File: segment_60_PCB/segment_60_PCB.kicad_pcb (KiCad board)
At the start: 2 copper layers, 119 parts, among them J1 MDB-9M, J2 #AVR-ISP-6, SW1 SW_Push_45deg, SW10 SW_Push_45deg, SW11 SW_Push_45deg, SW12 SW_Push_45deg, SW13 SW_Push_45deg, SW14 SW_Push_45deg, SW15 SW_Push_45deg, SW16 SW_Push_45deg, SW17 SW_Push_45deg, SW18 SW_Push_45deg, SW19 SW_Push_45deg, SW2 SW_Push_45deg, SW20 SW_Push_45deg, SW21 SW_Push_45deg, SW22 SW_Push_45deg, SW23 SW_Push_45deg, SW24 SW_Push_45deg, SW25 SW_Push_45deg, SW26 SW_Push_45deg, SW27 SW_Push_45deg, SW28 SW_Push_45deg, SW29 SW_Push_45deg, SW3 SW_Push_45deg, SW30 SW_Push_45deg, SW31 SW_Push_45deg, SW32 SW_Push_45deg, SW33 SW_Push_45deg, SW34 SW_Push_45deg, SW35 SW_Push_45deg, SW36 SW_Push_45deg, SW37 SW_Push_45deg, SW38 SW_Push_45deg, SW39 SW_Push_45deg, SW4 SW_Push_45deg, SW40 SW_Push_45deg, SW41 SW_Push_45deg, SW42 SW_Push_45deg, SW43 SW_Push_45deg, SW44 SW_Push_45deg, SW45 SW_Push_45deg, SW46 SW_Push_45deg, SW47 SW_Push_45deg, SW48 SW_Push_45deg, SW49 SW_Push_45deg, SW5 SW_Push_45deg, SW50 SW_Push_45deg, SW51 SW_Push_45deg, SW52 SW_Push_45deg, SW53 SW_Push_45deg, SW54 SW_Push_45deg, SW55 SW_Push_45deg, SW56 SW_Push_45deg, SW57 SW_Push_45deg, SW58 SW_Push_45deg, SW59 SW_Push_45deg, SW6 SW_Push_45deg, SW60 SW_Push_45deg, SW61 SW_Push_45deg, SW62 SW_Push_45deg, SW63 SW_Push_45deg, SW64 SW_Push_45deg, SW65 SW_Push_45deg, SW7 SW_Push_45deg, SW8 SW_Push_45deg, SW9 SW_Push_45deg, U1 ATmega328P-PU, U10 74HC365, U11 74HC365, U12 74HC365, U13 74HC365, U14 74HC365, U15 74HC365, U16 74HC365, U17 74HC365, U2 74HC138, U3 74HC138, U4 74HC365, U5 74HC365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

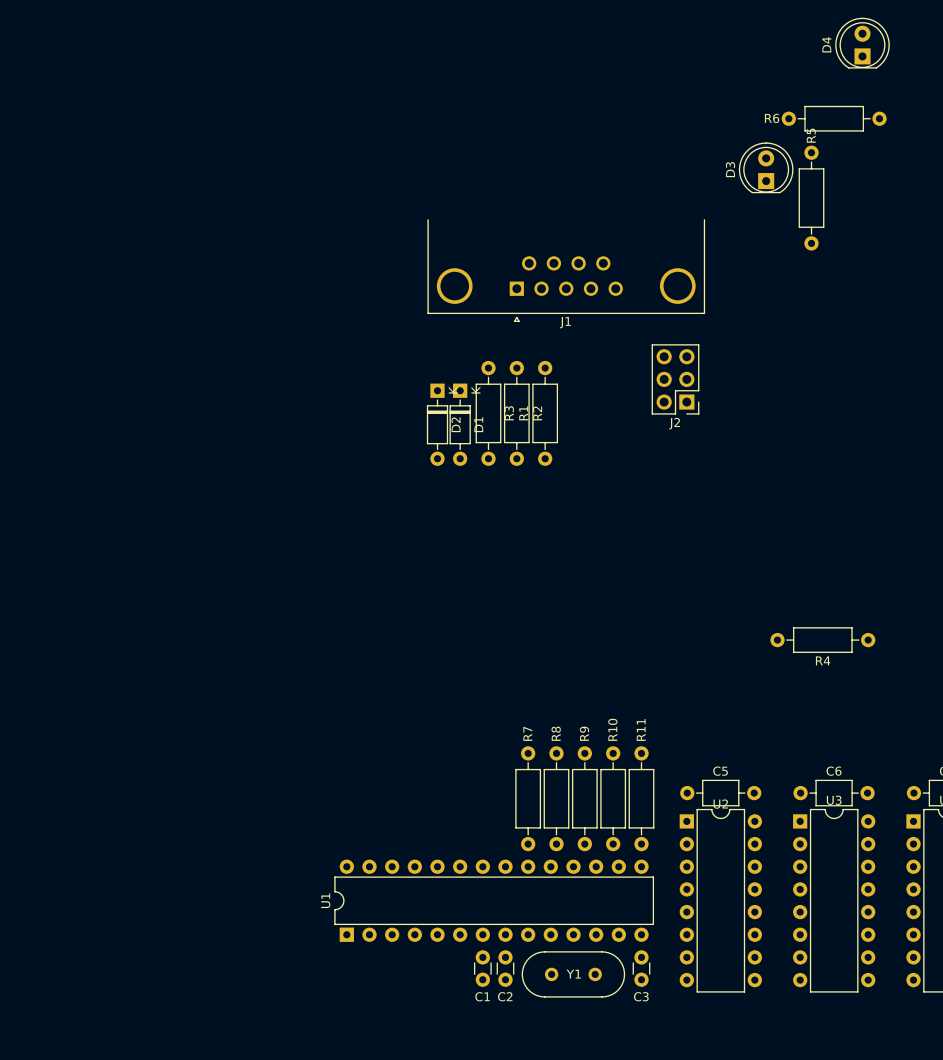
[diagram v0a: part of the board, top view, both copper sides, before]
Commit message: Continued organizing footprints and minor layout changes to control hardware.
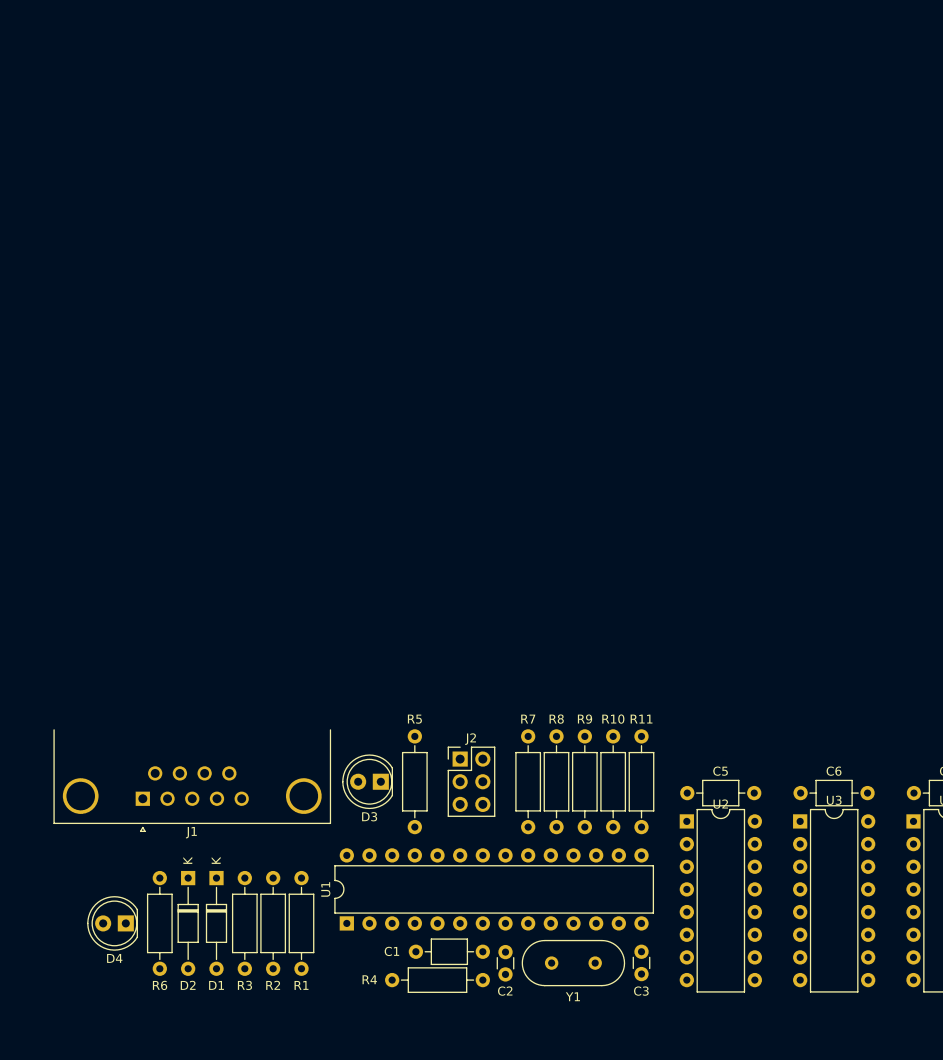
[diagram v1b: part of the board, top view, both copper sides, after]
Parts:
- C1: footprint Capacitor_THT:C_Disc_D3.0mm_W1.6mm_P2.50mm -> Capacitor_THT:C_Axial_L3.8mm_D2.6mm_P7.50mm_Horizontal
- D1, D2: footprint Diode_THT:D_DO-35_SOD27_P7.62mm_Horizontal -> Diode_THT:D_DO-35_SOD27_P10.16mm_Horizontal
- moved D4 127.5 mm to (93.3, 110.5), turned to 180 degrees
- moved R6 110.5 mm to (97.2, 105.4), turned to 270 degrees
- moved D3 80.0 mm to (121.9, 94.6), turned to 180 degrees
- moved R5 79.1 mm to (125.7, 89.5)
- moved J1 70.9 mm to (95.2, 96.5)
- moved R3 63.3 mm to (106.7, 105.4)
- moved R1 63.3 mm to (113.0, 115.6)
- moved R2 63.3 mm to (109.9, 105.4)
- moved D2 61.3 mm to (100.3, 105.4)
- moved D1 61.1 mm to (103.5, 105.4)
- moved R4 57.6 mm to (133.3, 116.8)
- moved J2 47.4 mm to (130.8, 92.1), turned to 0 degrees
- moved R10 1.91 mm to (148.0, 89.5)
- moved R11 1.91 mm to (151.1, 89.5)
- moved R7 1.91 mm to (138.4, 89.5)
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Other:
- net class Default: clearance 0.2 -> 0.4572; trace_width 0.25 -> 0.4572
- rule trace_clearance: 0.2 -> 0.4572

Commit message: Added remaining footprints, changed library paths to be relative.
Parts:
- added C4: 4.7u, Capacitor_THT:CP_Axial_L11.0mm_D5.0mm_P18.00mm_Horizontal, F.Cu at (103.5, 101.6)
- added F1: 100mA, Fuse:Fuse_Littelfuse_395Series, F.Cu at (113.0, 101.6)
- added SW66: SW_Push, Button_Switch_THT:SW_PUSH_6mm, F.Cu at (126.7, 97.8)
- added SW67: SW_Push, Button_Switch_THT:SW_PUSH_6mm, F.Cu at (118.1, 97.8)
- C1: footprint Capacitor_THT:C_Axial_L3.8mm_D2.6mm_P7.50mm_Horizontal -> Capacitor_THT:C_Axial_L3.8mm_D2.6mm_P10.00mm_Horizontal
- moved R5 28.3 mm to (133.3, 116.8), turned to 180 degrees
- moved J2 24.0 mm to (111.8, 106.7), turned to 270 degrees
- moved D3 22.5 mm to (116.8, 116.5), turned to 90 degrees
- moved R4 17.3 mm to (135.3, 99.7), turned to 90 degrees
- moved D4 16.4 mm to (108.6, 116.5), turned to 90 degrees
- moved R2 15.3 mm to (94.6, 106.0)
- moved R3 15.3 mm to (91.4, 106.0)
- moved D1 15.3 mm to (88.3, 106.0)
- moved D2 15.3 mm to (85.1, 106.0)
- moved R1 15.3 mm to (97.8, 116.2)
- moved R6 3.86 mm to (101.0, 106.0)
- moved J1 1.80 mm to (94.0, 95.2)
- moved C1 0.08 mm to (133.3, 113.7)
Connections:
- J1 pad 3: Net-(F1-Pad2) -> SCK
- J1 pad 4: SCK -> RST
- J1 pad 5: RST -> BOOT
- J1 pad 9: GND -> Net-(F1-Pad2)
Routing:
- net XTAL2: track 0.00 -> 12.0 mm
- net XTAL1: track 0.00 -> 10.5 mm
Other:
- net class Default: clearance 0.4572 -> 0.3; trace_width 0.4572 -> 0.3
- rule trace_clearance: 0.4572 -> 0.3
- board text added: "ADDR"
- board text added: "BANK A"
- board text added: "BANK B"
- board text added: "BOOT"
- board text added: "RESET"

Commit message: Tweaked layout.
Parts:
- moved F1 8.08 mm to (107.3, 107.3), turned to 0 degrees
- moved D4 6.81 mm to (105.4, 122.6)
- moved J2 6.25 mm to (109.2, 112.4)
- moved D3 6.06 mm to (117.5, 122.6)
- moved U1 5.75 mm to (117.5, 116.2)
- moved R10 5.75 mm to (147.3, 95.2)
- moved R7 5.75 mm to (137.8, 95.2)
- moved D1 5.75 mm to (87.6, 111.8)
- moved D2 5.75 mm to (84.5, 111.8)
- moved J1 5.75 mm to (93.3, 101.0)
- moved R1 5.75 mm to (97.2, 121.9)
- moved R6 5.75 mm to (100.3, 111.8)
- moved C2 5.75 mm to (135.3, 121.9)
- moved C4 5.75 mm to (102.9, 107.3)
- moved R11 5.75 mm to (150.5, 95.2)
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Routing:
- net XTAL2: track 12.0 -> 0.00 mm
- net XTAL1: track 10.5 -> 0.00 mm
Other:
- board text removed: "ADDR"
- board text removed: "BANK A"
- board text removed: "BANK B"

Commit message: Updated layout; changed row pullup resistors to a single resistor network
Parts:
- removed J2: #AVR-ISP-6, Connector_PinHeader_2.54mm:PinHeader_2x03_P2.54mm_Vertical
- removed R10, R11, R7, R8, R9: 10k, Resistor_THT:R_Axial_DIN0207_L6.3mm_D2.5mm_P10.16mm_Horizontal
- added RN1: 10k, Resistor_THT:R_Array_SIP7, F.Cu at (233.7, 102.9)
- J1: value MDB-9M -> BREAKOUT; footprint Connector_Dsub:DSUB-9_Female_Horizontal_P2.77x2.84mm_EdgePinOffset4.94mm_Housed_MountingHolesOffset7.48mm -> Connector_PinHeader_2.54mm:PinHeader_2x06_P2.54mm_Vertical
- moved D3 134.3 mm to (249.6, 98.1)
- moved R3 123.0 mm to (213.4, 122.6), turned to 90 degrees
- moved SW67 120.1 mm to (237.5, 99.1), turned to 180 degrees
- moved R2 116.7 mm to (210.2, 122.6), turned to 90 degrees
- moved D1 116.2 mm to (203.8, 112.4)
- moved D2 116.2 mm to (200.7, 112.4)
- moved R5 110.4 mm to (241.3, 102.9), turned to 0 degrees
- moved R1 110.3 mm to (207.0, 112.4), turned to 270 degrees
- moved J1 107.4 mm to (200.7, 106.0), turned to 90 degrees
- moved R4 102.3 mm to (233.7, 120.7), turned to 180 degrees
- moved C2 101.0 mm to (236.2, 120.0)
- moved C1 101.0 mm to (233.6, 117.5)
- moved U1 101.0 mm to (218.4, 114.3)
- moved Y1 101.0 mm to (241.4, 118.7)
- moved C3 101.0 mm to (251.5, 117.5)
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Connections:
- D1 pad 1: Net-(D1-Pad1) -> USB-
- D2 pad 1: Net-(D2-Pad1) -> USB+
- D3 pad 2: LED0 -> VCC
- J1 pad 2: MOSI -> Net-(F1-Pad2)
- J1 pad 4: RST -> MOSI
- J1 pad 5: BOOT -> RST
- J1 pad 7: Net-(D1-Pad1) -> TXD
- J1 pad 8: Net-(D2-Pad1) -> RXD
- J1 pad 9: Net-(F1-Pad2) -> BOOT
- R1 pad 1: VCC -> USB-
- R1 pad 2: Net-(D2-Pad1) -> VCC
- R2 pad 1: Net-(D2-Pad1) -> D-
- R2 pad 2: D- -> USB-
- R3 pad 1: Net-(D1-Pad1) -> D+
- R3 pad 2: D+ -> USB+
- R5 pad 2: GND -> LED0
- U1 pad 14: ROW0 -> /SEL4
- U1 pad 15: ROW1 -> BOOT
- U1 pad 2: BOOT -> RXD
- U1 pad 23: ROW2 -> ROW0
- U1 pad 24: ROW3 -> ROW1
- U1 pad 25: ROW4 -> ROW2
- U1 pad 26: Net-(U1-Pad26) -> ROW3
- U1 pad 27: Net-(U1-Pad27) -> ROW4
- U1 pad 28: Net-(U1-Pad28) -> ROW5
- U1 pad 3: Net-(U1-Pad3) -> TXD
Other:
- board text removed: "BOOT"
- board text removed: "RESET"

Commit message: added border, changed J1 footprint and model
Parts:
- J1: footprint Connector_PinHeader_2.54mm:PinHeader_2x06_P2.54mm_Vertical -> Connector_IDC:IDC-Header_2x06_P2.54mm_Vertical
- moved F1 15.3 mm to (193.4, 119.4), turned to 90 degrees
- moved SW67 5.08 mm to (237.6, 104.1)
- moved SW66 5.03 mm to (224.9, 104.1)
- moved R5 4.44 mm to (241.3, 107.3)
- moved RN1 4.44 mm to (233.7, 107.3)
- moved D3 4.09 mm to (249.6, 102.2)
- moved C1 3.81 mm to (233.6, 121.3)
- moved C2 3.81 mm to (236.2, 123.8)
- moved C3 3.81 mm to (251.5, 121.3)
- moved U1 3.81 mm to (218.4, 118.1)
- moved Y1 3.81 mm to (241.4, 122.6)
- moved R4 3.81 mm to (233.7, 124.5)
- moved R6 3.70 mm to (197.5, 114.3)
- moved J1 3.70 mm to (197.5, 108.0)
- moved U12 3.17 mm to (281.9, 107.3)
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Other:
- board outline added: 285.8 x 126.4 mm
- board text added: "BANK A"
- board text added: "BANK B"
- board text added: "BOOT"
- board text added: "CPU"
- board text added: "DEMUX"
- board text added: "FUNC"
- board text added: "IO PORT A"
- board text added: "POWER"
- board text added: "RESET"

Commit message: Updated switch footprints to include 3D models
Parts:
- moved SW67 6.45 mm to (238.8, 97.8)
- moved C2 6.35 mm to (236.2, 117.5)
- moved C3 6.35 mm to (251.5, 115.0)
- moved C4 6.35 mm to (188.0, 99.7)
- moved J1 6.35 mm to (197.5, 101.6)
- moved Y1 6.35 mm to (241.4, 116.2)
- moved C1 6.35 mm to (233.6, 114.9)
- moved C10 6.35 mm to (123.2, 95.9)
- moved C11 6.35 mm to (135.9, 95.9)
- moved C12 6.35 mm to (148.6, 95.9)
- moved C13 6.35 mm to (161.3, 95.9)
- moved C14 6.35 mm to (174.0, 95.9)
- moved C15 6.35 mm to (282.0, 95.9)
- moved C16 6.35 mm to (294.7, 95.9)
- moved C17 6.35 mm to (307.4, 95.9)
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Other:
- board size 285.8 x 126.4 mm -> 285.8 x 133.4 mm
- board text added: "SERIAL"
- board text removed: "IO PORT A"

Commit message: Added power pours for VCC
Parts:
- removed F1: 100mA, Fuse:Fuse_Littelfuse_395Series
- removed the R6 at (197.5, 108.0)
- added H1: TOP, MountingHole:MountingHole_3.2mm_M3, F.Cu at (80.0, 92.7)
- added H10: MATRIX, MountingHole:MountingHole_3.2mm_M3_Pad, F.Cu at (238.1, 212.7)
- added H11: MATRIX, MountingHole:MountingHole_3.2mm_M3_Pad, F.Cu at (314.3, 146.7)
- added H12: MATRIX, MountingHole:MountingHole_3.2mm_M3_Pad, F.Cu at (335.9, 212.7)
- added H2: TOP, MountingHole:MountingHole_3.2mm_M3, F.Cu at (358.1, 92.7)
- added H3: TOP, MountingHole:MountingHole_3.2mm_M3, F.Cu at (80.0, 118.4)
- added H4: TOP, MountingHole:MountingHole_3.2mm_M3, F.Cu at (358.1, 118.4)
- added H5: MATRIX, MountingHole:MountingHole_3.2mm_M3_Pad, F.Cu at (123.8, 146.7)
- added H6: MATRIX, MountingHole:MountingHole_3.2mm_M3_Pad, F.Cu at (102.2, 212.7)
- added H7: MATRIX, MountingHole:MountingHole_3.2mm_M3_Pad, F.Cu at (200.0, 146.7)
- added H8: MATRIX, MountingHole:MountingHole_3.2mm_M3_Pad, F.Cu at (200.0, 212.7)
- added H9: MATRIX, MountingHole:MountingHole_3.2mm_M3_Pad, F.Cu at (238.1, 146.7)
- added R4: 4.7k, Resistor_THT:R_Axial_DIN0207_L6.3mm_D2.5mm_P10.16mm_Horizontal, F.Cu at (195.9, 118.1)
- added R5: 4.7k, Resistor_THT:R_Axial_DIN0207_L6.3mm_D2.5mm_P10.16mm_Horizontal, F.Cu at (199.1, 118.1)
- added R8: 220R, Resistor_THT:R_Axial_DIN0207_L6.3mm_D2.5mm_P10.16mm_Horizontal, F.Cu at (192.7, 108.0)
- C1: footprint Capacitor_THT:C_Axial_L3.8mm_D2.6mm_P10.00mm_Horizontal -> Segment_Footprints:C_Axial_L3.8mm_D2.6mm_P10.16mm_Horizontal
- C10, C11, C12, C13, C14, C15, C16, C17, C18, C19, C20, C5, C6, C7, C8, C9: footprint Capacitor_THT:C_Axial_L3.8mm_D2.6mm_P7.50mm_Horizontal -> Segment_Footprints:C_Axial_L3.8mm_D2.6mm_P7.62mm_Horizontal
- moved SW66 7.39 mm to (219.1, 93.3), turned to 0 degrees
- moved SW67 6.33 mm to (234.3, 93.3), turned to 0 degrees
- moved C1 4.36 mm to (229.2, 114.9)
- moved C18 3.76 mm to (323.9, 95.9)
- moved C5 3.76 mm to (260.4, 95.9), turned to 180 degrees
- moved C12 3.76 mm to (152.4, 95.9)
- moved C14 3.76 mm to (177.8, 95.9)
- moved C10 3.76 mm to (127.0, 95.9)
- moved C7 3.76 mm to (88.9, 95.9)
- moved C11 3.76 mm to (139.7, 95.9)
- moved C13 3.76 mm to (165.1, 95.9)
- moved C15 3.76 mm to (285.8, 95.9)
- moved C16 3.76 mm to (298.4, 95.9)
- moved C17 3.76 mm to (311.1, 95.9)
- moved C19 3.76 mm to (336.6, 95.9)
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- renumbered R4 to R6, R5 to R7
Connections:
- J1 pad 2: Net-(F1-Pad2) -> VCC
- J1 pad 7: TXD -> SDA
- J1 pad 8: RXD -> SCL
- U1 pad 2: RXD -> ROW4
- U1 pad 27: ROW4 -> SDA
- U1 pad 28: ROW5 -> SCL
- U1 pad 3: TXD -> ROW5
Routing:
- net VCC: track 0.00 -> 87.6 mm
- net RST: track 0.00 -> 55.0 mm
- net MOSI: track 0.00 -> 51.2 mm
- net BOOT: track 0.00 -> 50.4 mm
- net SCL: track 0.00 -> 41.8 mm
- net SDA: track 0.00 -> 29.4 mm
- net /SEL1: track 0.00 -> 29.2 mm
- net USB+: track 0.00 -> 25.9 mm
- net /SEL2: track 0.00 -> 25.6 mm
- net /SEL3: track 0.00 -> 23.1 mm
- net D-: track 0.00 -> 22.7 mm
- net D+: track 0.00 -> 17.8 mm
- net ROW5: track 0.00 -> 16.5 mm
- net USB-: track 0.00 -> 14.6 mm
- net /SEL0: track 0.00 -> 13.8 mm
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- added copper zone on B.Cu, net GND
- added copper zone on F.Cu, net VCC
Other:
- net class Default: clearance 0.3 -> 0.313; trace_width 0.3 -> 0.313
- rule trace_clearance: 0.3 -> 0.313
- board text added: "DO NOT OBSTRUCT"
- board text added: "SERIAL BREAKOUT"
- board text removed: "CPU"
- board text removed: "SERIAL"

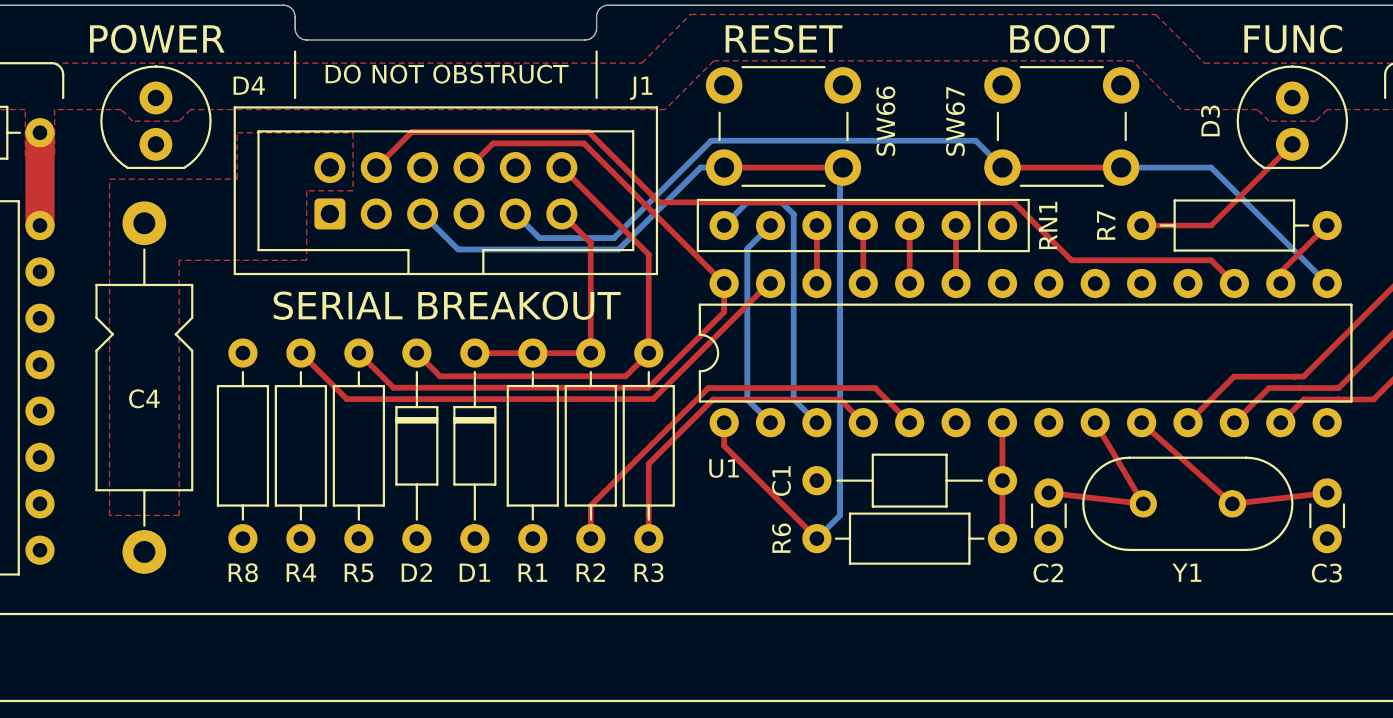
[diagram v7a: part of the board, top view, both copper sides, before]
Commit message: Routed some more logic lines; continued adding and chaning VCC pours
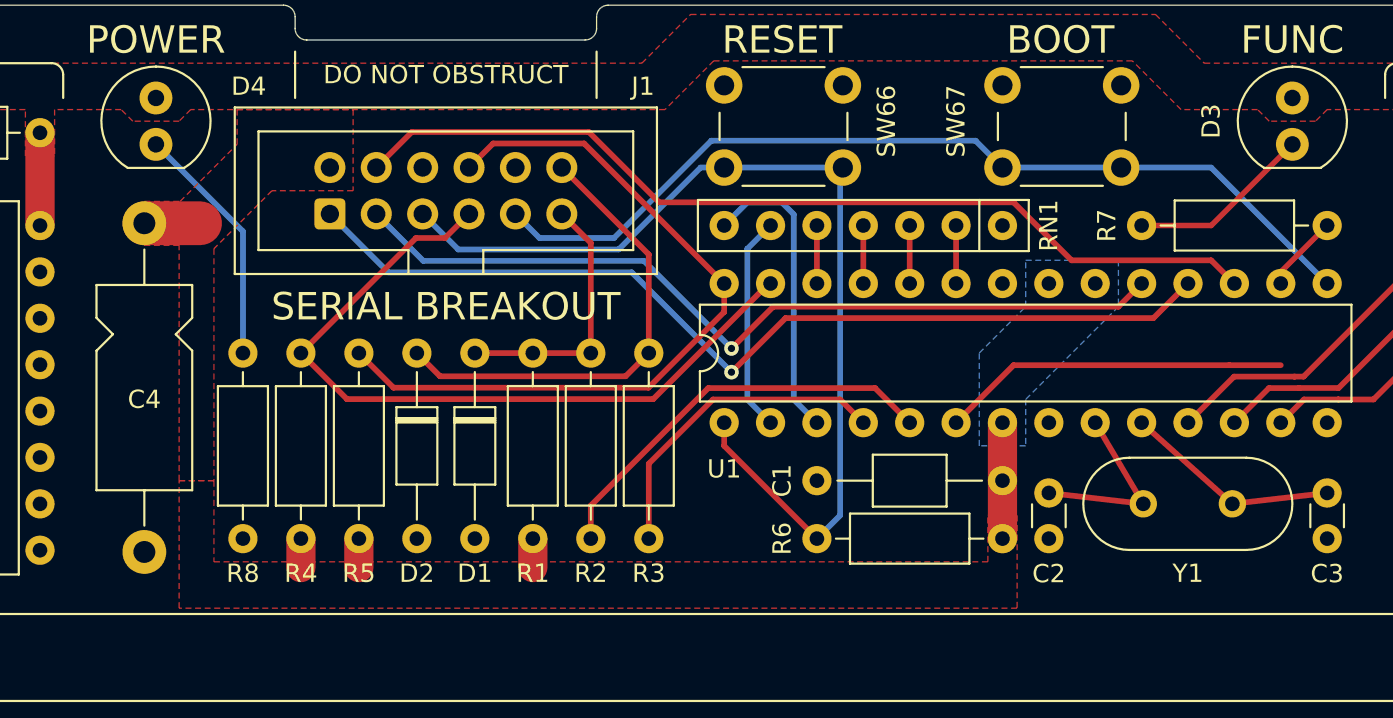
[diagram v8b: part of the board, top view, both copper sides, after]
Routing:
- net MISO: track 0.00 -> 52.6 mm, vias 0 -> 1
- net SCK: track 0.00 -> 46.4 mm, vias 0 -> 1
- net /SEL0: track 13.8 -> 32.8 mm
- net Net-(D4-Pad1): track 0.00 -> 13.4 mm
- net SDA: track 29.4 -> 41.7 mm
- net VCC: track 87.6 -> 95.4 mm
- added copper zone on B.Cu, net VCC
